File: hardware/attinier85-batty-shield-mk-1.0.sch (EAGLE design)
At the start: 6 parts, among them U1 ATTINIEST85_SHIELDV2

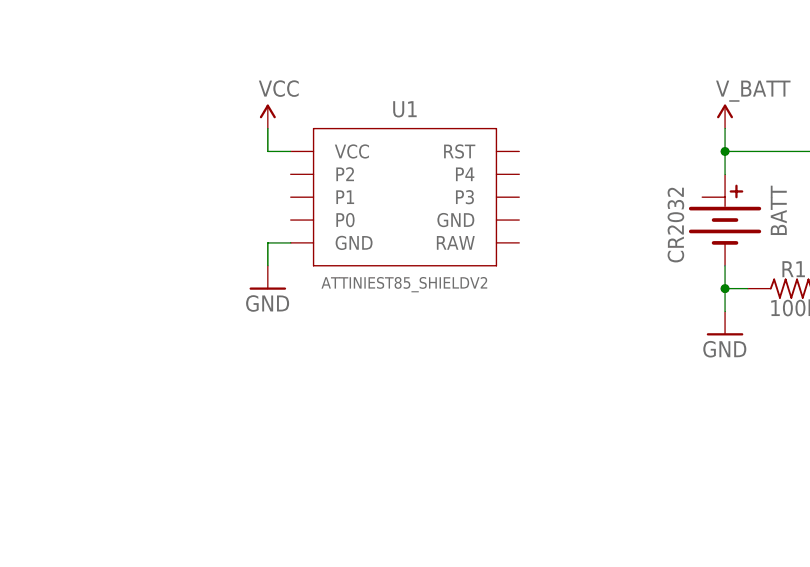
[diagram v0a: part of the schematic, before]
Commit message: renaming parts
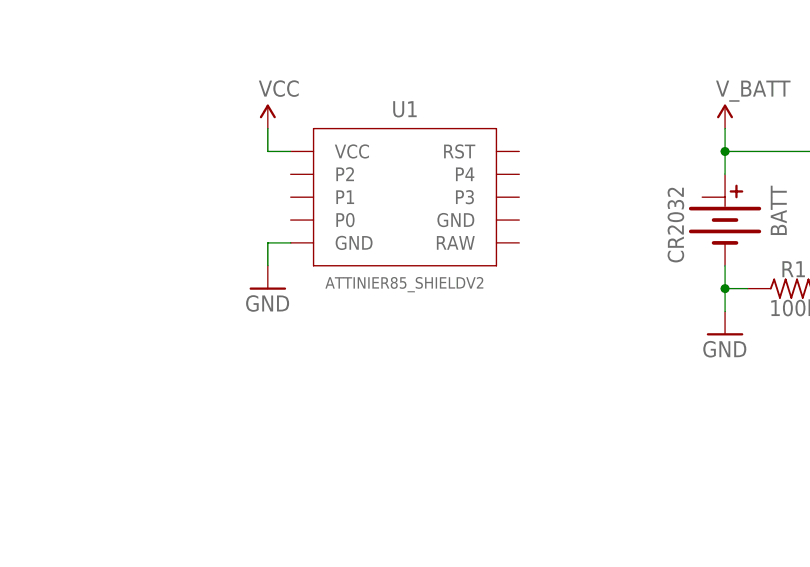
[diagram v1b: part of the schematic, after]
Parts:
- U1: value ATTINIEST85_SHIELDV2 -> ATTINIER85_SHIELDV2; device A_butts:ATTINIEST85_SHIELDV2 -> A_butts:ATTINIER85_SHIELDV2
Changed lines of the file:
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@@
 <parts>
 <part name="FRAME1" library="A_butts" deviceset="FRAME-LETTER" device="NO_PACKAGE"/>
-<part name="U1" library="A_butts" deviceset="ATTINIEST85_SHIELD" device="V2"/>
+<part name="U1" library="A_butts" deviceset="ATTINIER85_SHIELD" device="V2"/>
 <part name="SUPPLY1" library="A_butts" deviceset="VCC" device=""/>
 <part name="SUPPLY2" library="A_butts" deviceset="V_BATT" device=""/>

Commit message: cleaning up version spoo
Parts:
- removed D1: 10V, A_butts:DIODE-ZENER7.62MM-PTH
- removed Q1: (no value), A_butts:MOSFET-PCHANNELTO-92-INLINE-DGS
- removed R1: 100k, A_butts:RESISTORPTH-AXIAL-7.62MM
- added JP1: VCC RAW, A_butts:JUMPER-PAD-3-NOFULL_BOX_SILK
- added PWR: SWITCH-SPDTPTH-RA-2MM, A_butts:SWITCH-SPDTPTH-RA-2MM
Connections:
- removed net N$1: D1.C, Q1.G, R1.2
- removed net V_BATT: BATT.+, D1.A, Q1.D
- new net RAW: JP1.1, U1.RAW
- new net VBATT: BATT.+, BATT.+1, PWR.COM
- net GND: now also U1.GND@1; no longer R1.1
- net VCC: now also JP1.2, JP1.3, PWR.NC; no longer Q1.S
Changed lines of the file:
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@@
 <part name="FRAME1" library="A_butts" deviceset="FRAME-LETTER" device="NO_PACKAGE"/>
 <part name="U1" library="A_butts" deviceset="ATTINIER85_SHIELD" device="V2"/>
-<part name="SUPPLY1" library="A_butts" deviceset="VCC" device=""/>
-<part name="SUPPLY2" library="A_butts" deviceset="V_BATT" device=""/>
 <part name="GND1" library="A_butts" deviceset="GND" device=""/>
 <part name="BATT" library="A_butts" deviceset="BATTERY-COIN" device="CR2032_SMD" value="CR2032"/>
-<part name="D1" library="A_butts" deviceset="DIODE-ZENER" device="7.62MM-PTH" value="10V"/>
-<part name="R1" library="A_butts" deviceset="RESISTOR" device="PTH-AXIAL-7.62MM" value="100k"/>
-<part name="Q1" library="A_butts" deviceset="MOSFET-PCHANNEL" device="TO-92-INLINE-DGS"/>
-<part name="SUPPLY3" library="A_butts" deviceset="V_BATT" device=""/>
-<part name="SUPPLY4" library="A_butts" deviceset="VCC" device=""/>
 <part name="GND2" library="A_butts" deviceset="GND" device=""/>
+<part name="PWR" library="A_butts" deviceset="SWITCH-SPDT" device="PTH-RA-2MM"/>
+<part name="JP1" library="A_butts" deviceset="JUMPER-PAD-3-NO" device="FULL_BOX_SILK" value="VCC   RAW"/>
 </parts>
 <sheets>
@@
 <instance part="FRAME1" gate="V" x="154.94" y="0"/>
 <instance part="U1" gate="G$1" x="63.5" y="73.66"/>
-<instance part="SUPPLY1" gate="G$1" x="48.26" y="81.28"/>
-<instance part="SUPPLY2" gate="G$1" x="99.06" y="81.28"/>
 <instance part="GND1" gate="1" x="99.06" y="58.42"/>
 <instance part="BATT" gate="G$1" x="99.06" y="71.12" rot="R270"/>
-<instance part="D1" gate="G$1" x="114.3" y="71.12" rot="R270"/>
-<instance part="R1" gate="G$1" x="106.68" y="63.5"/>
-<instance part="Q1" gate="G$1" x="121.92" y="78.74" rot="R90"/>
-<instance part="SUPPLY3" gate="G$1" x="132.08" y="66.04"/>
-<instance part="SUPPLY4" gate="G$1" x="129.54" y="81.28"/>
 <instance part="GND2" gate="1" x="48.26" y="63.5"/>
+<instance part="PWR" gate="G$1" x="111.76" y="81.28"/>
+<instance part="JP1" gate="G$1" x="119.38" y="91.44" smashed="yes" rot="R90">
+<attribute name="NAME" x="121.92" y="86.741" size="1.778" layer="95"/>
+<attribute name="VALUE" x="119.38" y="94.615" size="1.778" layer="96" align="bottom-center"/>
+</instance>
 </instances>
 <busses>
@@
 <pinref part="BATT" gate="G$1" pin="-"/>
 <pinref part="GND1" gate="1" pin="GND"/>
-<wire x1="99.06" y1="60.96" x2="99.06" y2="63.5" width="0.1524" layer="91"/>
-<pinref part="R1" gate="G$1" pin="1"/>
-<wire x1="99.06" y1="63.5" x2="99.06" y2="66.04" width="0.1524" layer="91"/>
-<wire x1="99.06" y1="63.5" x2="101.6" y2="63.5" width="0.1524" layer="91"/>
-<junction x="99.06" y="63.5"/>
+<wire x1="99.06" y1="60.96" x2="99.06" y2="66.04" width="0.1524" layer="91"/>
 </segment>
 <segment>
@@
 <wire x1="48.26" y1="68.58" x2="50.8" y2="68.58" width="0.1524" layer="91"/>
 </segment>
+<segment>
+<pinref part="U1" gate="G$1" pin="GND@1"/>
+<wire x1="78.74" y1="71.12" x2="76.2" y2="71.12" width="0.1524" layer="91"/>
+<label x="78.74" y="71.12" size="1.27" layer="95" xref="yes"/>
+</segment>
 </net>
-<net name="V_BATT" class="0">
+<net name="VBATT" class="0">
 <segment>
-<pinref part="SUPPLY2" gate="G$1" pin="V_BATT"/>
-<wire x1="99.06" y1="81.28" x2="99.06" y2="78.74" width="0.1524" layer="91"/>
-<pinref part="Q1" gate="G$1" pin="D"/>
-<wire x1="99.06" y1="78.74" x2="114.3" y2="78.74" width="0.1524" layer="91"/>
-<pinref part="D1" gate="G$1" pin="A"/>
-<wire x1="114.3" y1="78.74" x2="116.84" y2="78.74" width="0.1524" layer="91"/>
-<wire x1="114.3" y1="73.66" x2="114.3" y2="78.74" width="0.1524" layer="91"/>
-<junction x="114.3" y="78.74"/>
+<pinref part="BATT" gate="G$1" pin="+1"/>
+<wire x1="96.52" y1="73.66" x2="96.52" y2="76.2" width="0.1524" layer="91"/>
 <pinref part="BATT" gate="G$1" pin="+"/>
-<wire x1="99.06" y1="76.2" x2="99.06" y2="78.74" width="0.1524" layer="91"/>
-<junction x="99.06" y="78.74"/>
+<wire x1="96.52" y1="76.2" x2="99.06" y2="76.2" width="0.1524" layer="91"/>
+<wire x1="99.06" y1="76.2" x2="99.06" y2="81.28" width="0.1524" layer="91"/>
+<junction x="99.06" y="76.2"/>
+<pinref part="PWR" gate="G$1" pin="COM"/>
+<wire x1="99.06" y1="81.28" x2="106.68" y2="81.28" width="0.1524" layer="91"/>
+</segment>
+</net>
+<net name="RAW" class="0">
+<segment>
+<pinref part="U1" gate="G$1" pin="RAW"/>
+<wire x1="78.74" y1="68.58" x2="76.2" y2="68.58" width="0.1524" layer="91"/>
+<label x="78.74" y="68.58" size="1.27" layer="95" xref="yes"/>
+</segment>
+<segment>
+<pinref part="JP1" gate="G$1" pin="1"/>
+<wire x1="111.76" y1="91.44" x2="114.3" y2="91.44" width="0.1524" layer="91"/>
+<label x="111.76" y="91.44" size="1.27" layer="95" rot="R180" xref="yes"/>
 </segment>
 </net>
 <net name="VCC" class="0">
 <segment>
-<pinref part="SUPPLY1" gate="G$1" pin="VCC"/>
-<wire x1="48.26" y1="81.28" x2="48.26" y2="78.74" width="0.1524" layer="91"/>
 <pinref part="U1" gate="G$1" pin="VCC"/>
 <wire x1="48.26" y1="78.74" x2="50.8" y2="78.74" width="0.1524" layer="91"/>
+<label x="48.26" y="78.74" size="1.27" layer="95" rot="R180" xref="yes"/>
 </segment>
 <segment>
-<pinref part="SUPPLY4" gate="G$1" pin="VCC"/>
-<wire x1="129.54" y1="81.28" x2="129.54" y2="78.74" width="0.1524" layer="91"/>
-<pinref part="Q1" gate="G$1" pin="S"/>
-<wire x1="129.54" y1="78.74" x2="127" y2="78.74" width="0.1524" layer="91"/>
-</segment>
-</net>
-<net name="N$1" class="0">
-<segment>
-<pinref part="R1" gate="G$1" pin="2"/>
-<pinref part="Q1" gate="G$1" pin="G"/>
-<wire x1="111.76" y1="63.5" x2="114.3" y2="63.5" width="0.1524" layer="91"/>
-<wire x1="114.3" y1="63.5" x2="121.92" y2="63.5" width="0.1524" layer="91"/>
-<wire x1="121.92" y1="63.5" x2="121.92" y2="71.12" width="0.1524" layer="91"/>
-<pinref part="D1" gate="G$1" pin="C"/>
-<wire x1="114.3" y1="63.5" x2="114.3" y2="68.58" width="0.1524" layer="91"/>
-<junction x="114.3" y="63.5"/>
+<pinref part="JP1" gate="G$1" pin="3"/>
+<wire x1="127" y1="91.44" x2="124.46" y2="91.44" width="0.1524" layer="91"/>
+<label x="127" y="91.44" size="1.27" layer="95" xref="yes"/>
+<pinref part="PWR" gate="G$1" pin="NC"/>
+<wire x1="116.84" y1="83.82" x2="119.38" y2="83.82" width="0.1524" layer="91"/>
+<pinref part="JP1" gate="G$1" pin="2"/>
+<wire x1="119.38" y1="83.82" x2="119.38" y2="86.36" width="0.1524" layer="91"/>
+<wire x1="119.38" y1="86.36" x2="119.38" y2="91.44" width="0.1524" layer="91"/>
+<junction x="119.38" y="86.36"/>
+<wire x1="119.38" y1="91.44" x2="124.46" y2="91.44" width="0.1524" layer="91"/>
+<junction x="124.46" y="91.44"/>
 </segment>
 </net>
@@
 </sheet>
 </sheets>
+<errors>
+</errors>
 </schematic>
 </drawing>
